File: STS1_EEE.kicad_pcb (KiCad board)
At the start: 4 copper layers, 81.1 x 85 mm, 43 parts, among them J1 Conn_02x20_Odd_Even, J2 Conn_02x20_Odd_Even, SW1 SW_SPST, U1 coordinate_system, U2 ST_Logo, U3 MP28167GQ, U4 1047

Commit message: Add EDU_HEARTBEAT adn EDU_UPDATE connections
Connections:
- J2 pad 37: unconnected-(J2-Pin_37-Pad37) -> EDU_Heartbeat
- J2 pad 39: unconnected-(J2-Pin_39-Pad39) -> EDU_UPDATE
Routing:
- net EDU_Heartbeat: track 2.00 -> 55.0 mm
- net EDU_UPDATE: track 2.00 -> 54.1 mm
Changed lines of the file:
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@@
 			(layers "*.Cu" "*.Mask")
 			(remove_unused_layers no)
-			(net "unconnected-(J2-Pin_37-Pad37)")
+			(net "EDU_Heartbeat")
 			(pinfunction "Pin_37_37")
-			(pintype "passive+no_connect")
+			(pintype "passive")
 		)
 		(pad "38" thru_hole circle
@@
 			(layers "*.Cu" "*.Mask")
 			(remove_unused_layers no)
-			(net "unconnected-(J2-Pin_39-Pad39)")
+			(net "EDU_UPDATE")
 			(pinfunction "Pin_39_39")
-			(pintype "passive+no_connect")
+			(pintype "passive")
 		)
 		(pad "40" thru_hole circle
@@
 		(sheetname "/powersupply/")
 		(sheetfile "powersupply.kicad_sch")
+		(units
+			(unit
+				(name "A")
+				(pins "1" "2" "3" "4")
+			)
+		)
 		(attr through_hole)
 		(duplicate_pad_numbers_are_jumpers no)
@@
 	)
 	(segment
+		(start 167.905 107.3)
+		(end 169.225 105.98)
+		(width 0.762)
+		(layer "B.Cu")
+		(net "EDU_Heartbeat")
+	)
+	(segment
+		(start 129.5 107.3)
+		(end 167.905 107.3)
+		(width 0.762)
+		(layer "B.Cu")
+		(net "EDU_Heartbeat")
+	)
+	(segment
+		(start 120.5 98.3)
+		(end 129.5 107.3)
+		(width 0.762)
+		(layer "B.Cu")
+		(net "EDU_Heartbeat")
+	)
+	(segment
 		(start 118.5 100.3)
 		(end 120.5 100.3)
@@
 		(net "EDU_UPDATE")
 	)
+	(segment
+		(start 128.72 108.52)
+		(end 169.225 108.52)
+		(width 0.762)
+		(layer "B.Cu")
+		(net "EDU_UPDATE")
+	)
+	(segment
+		(start 120.5 100.3)
+		(end 128.72 108.52)
+		(width 0.762)
+		(layer "B.Cu")
+		(net "EDU_UPDATE")
+	)

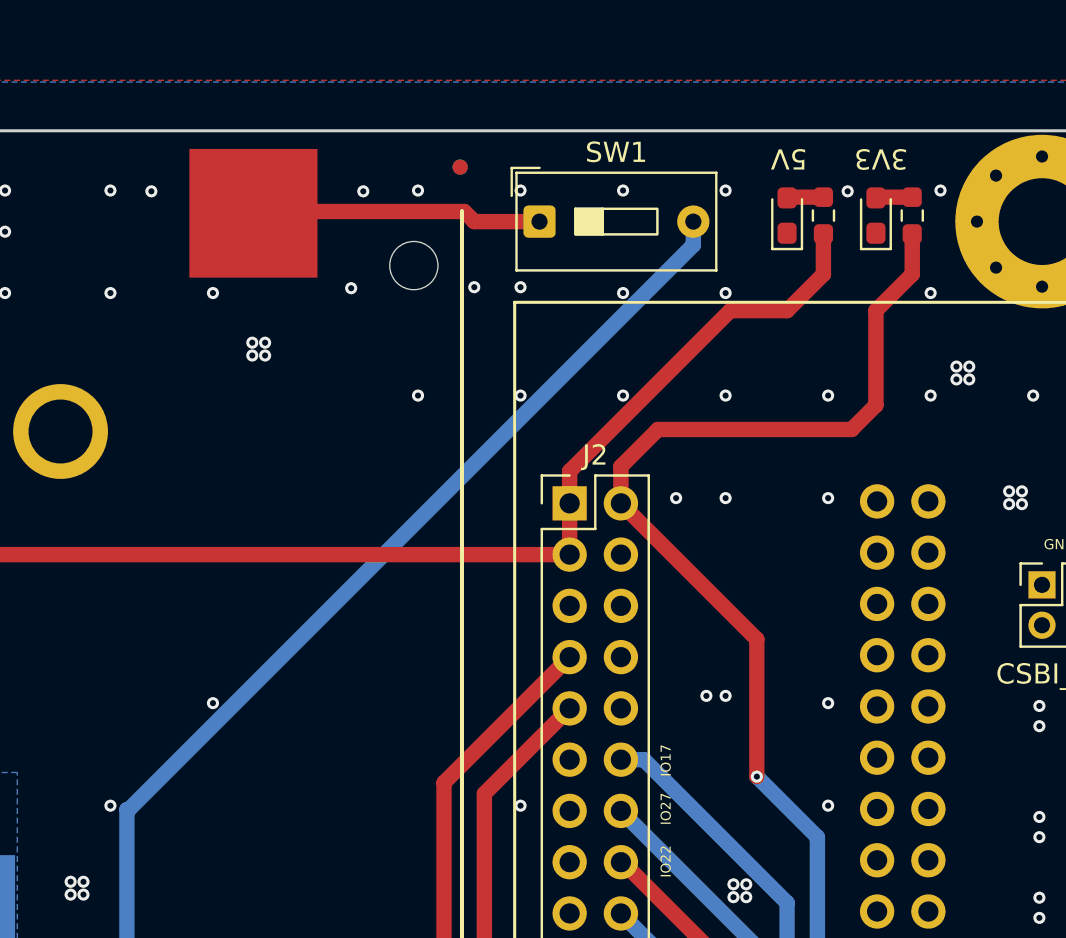
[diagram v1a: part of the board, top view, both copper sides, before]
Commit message: Replace the switch with the real one: 633-CS12ANW03
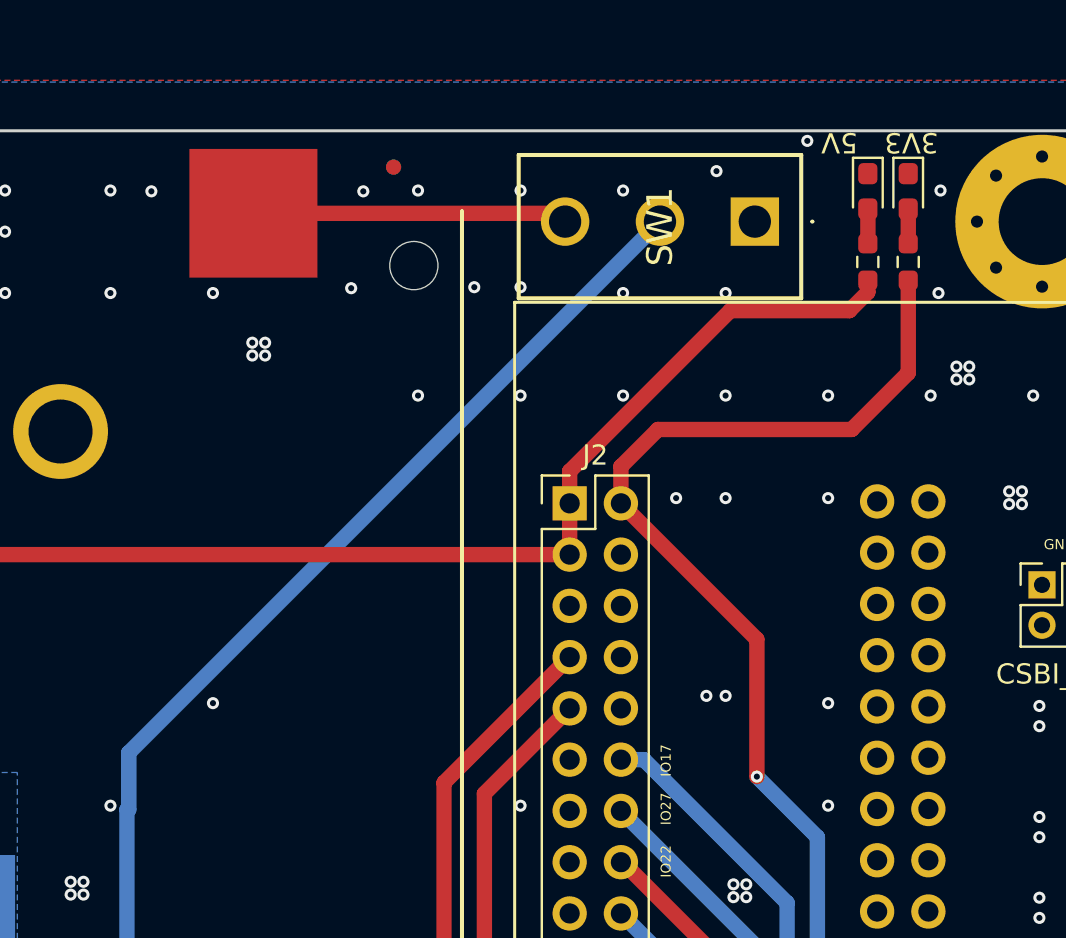
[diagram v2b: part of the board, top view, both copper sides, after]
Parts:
- SW1: footprint Button_Switch_THT:SW_DIP_SPSTx01_Slide_9.78x4.72mm_W7.62mm_P2.54mm -> STS_EEE:CS12ANW03
- moved SW1 10.7 mm to (178.4, 46.3), turned to 90 degrees
- moved D4 4.18 mm to (184.0, 44.8), turned to -90 degrees
- moved FID3 3.30 mm to (160.5, 43.6)
- moved FID4 3.30 mm to (160.5, 43.6)
- moved R4 3.18 mm to (184.0, 48.3)
- moved R3 2.31 mm to (186.0, 48.3)
- moved D3 2.00 mm to (186.0, 44.8), turned to -90 degrees
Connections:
- SW1 pad 1: Net-(SW1-A) -> unconnected-(SW1-NC-Pad1)
- U4 pad 3: Net-(SW1-A) -> Net-(SW1-NO)
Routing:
- net Net-(SW1-NO): track 0.00 -> 16.2 mm
- net Net-(SW1-A): track 14.5 -> 0.00 mm
- net Pi_3V3: track 97.4 -> 95.0 mm
- net VBAT: track 68.4 -> 67.7 mm

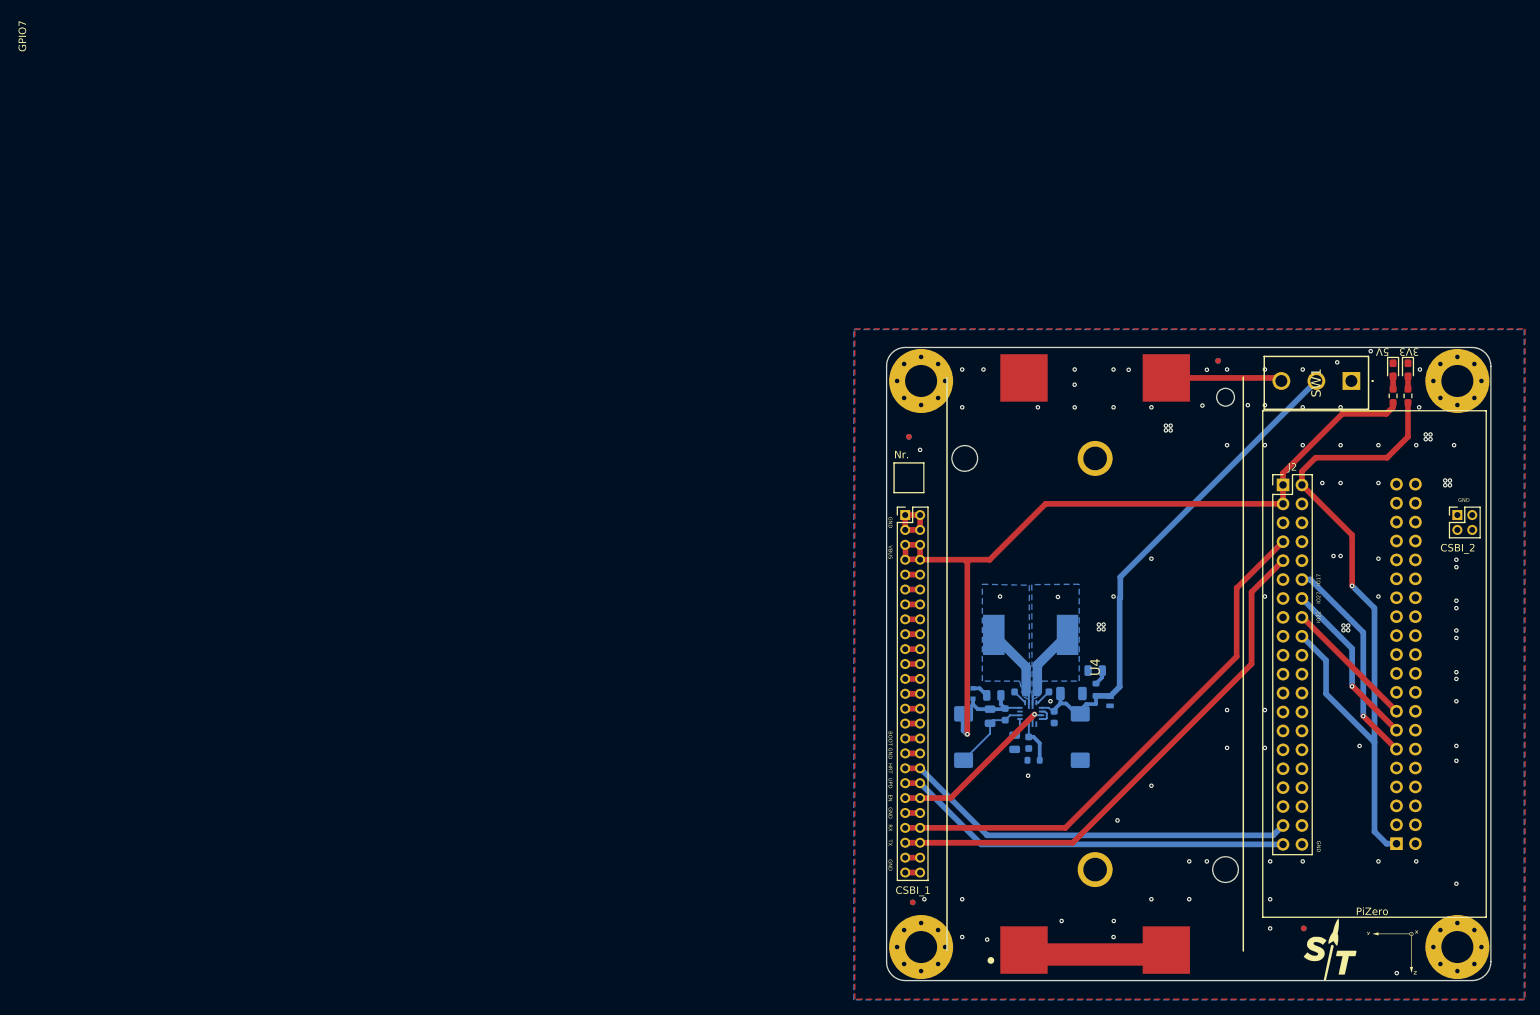
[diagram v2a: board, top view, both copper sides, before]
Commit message: Fix DRC errors and clean-up around the DC-DC circuit
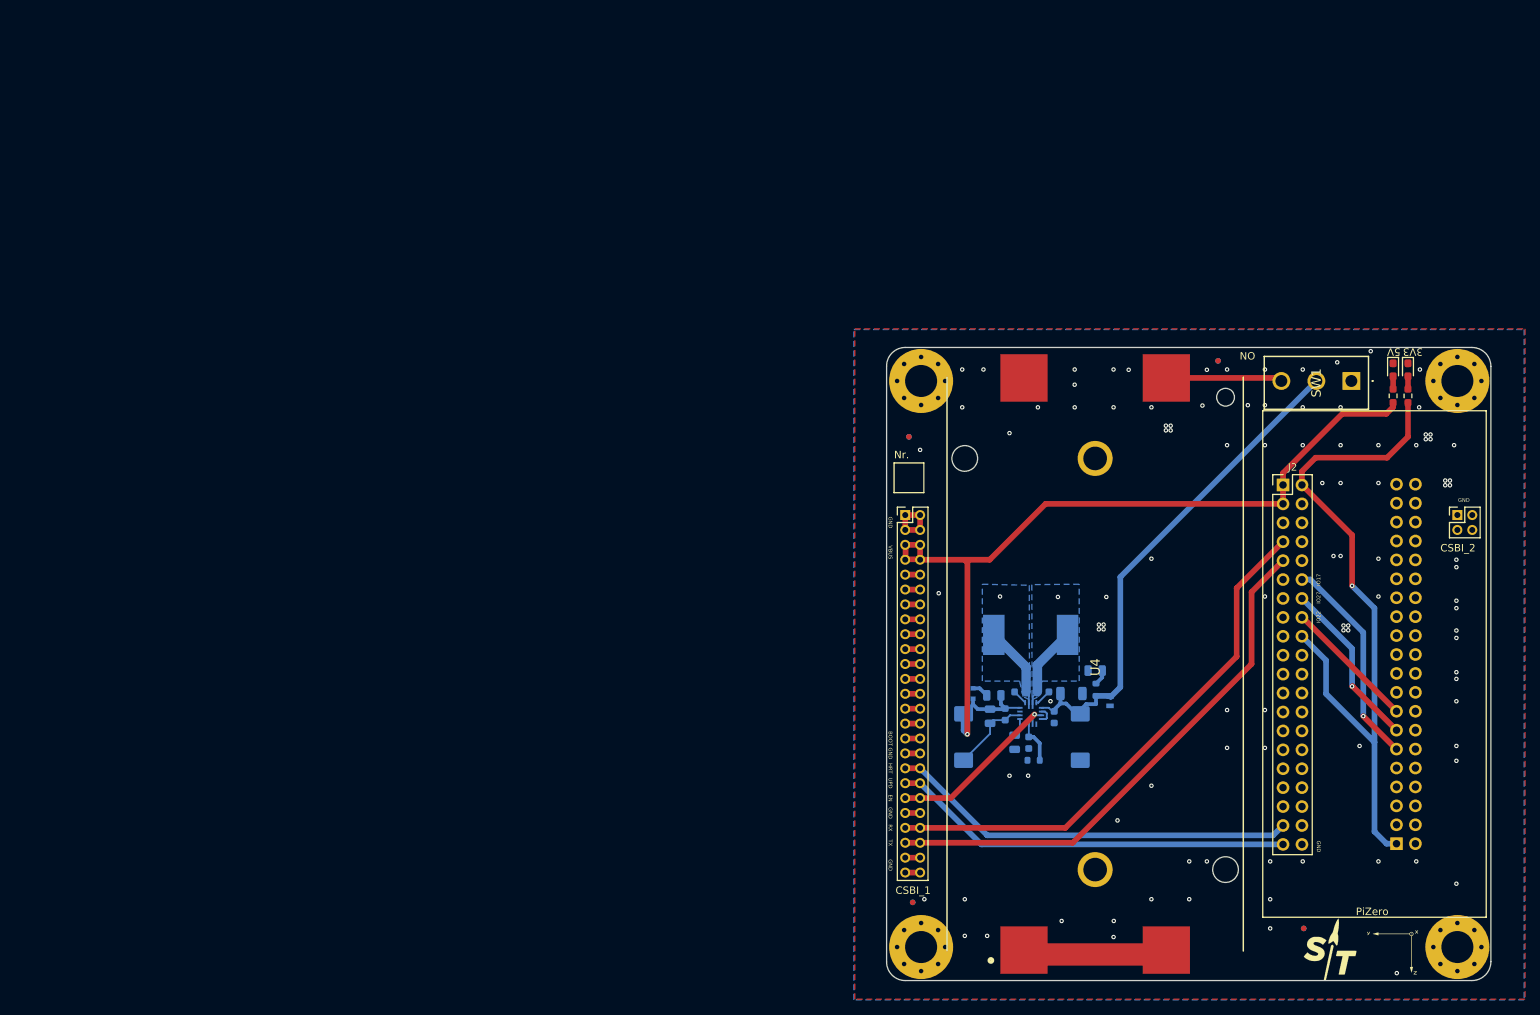
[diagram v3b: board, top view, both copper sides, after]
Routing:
- net GPIO27: vias 2 -> 1
- net GND: vias 103 -> 106
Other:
- rule pad_to_mask_clearance: 0.19 -> 0.05
- board text added: "ON"
- board text removed: "GPIO7"
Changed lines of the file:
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@@
 			(dielectric_constraints no)
 		)
-		(pad_to_mask_clearance 0.19)
+		(pad_to_mask_clearance 0.05)
 		(solder_mask_min_width 0.25)
 		(allow_soldermask_bridges_in_footprints no)
@@
 			(at 0 -1.68 90)
 			(layer "B.Fab")
+			(hide yes)
 			(effects
 				(font
@@
 			(at 0 -1.43 0)
 			(layer "B.Fab")
+			(hide yes)
 			(effects
 				(font
@@
 			)
 		)
-		(attr through_hole)
+		(attr smd)
 		(duplicate_pad_numbers_are_jumpers no)
 		(fp_line
@@
 			(at 0 -1.778 0)
 			(layer "B.SilkS")
+			(hide yes)
 			(effects
 				(font
@@
 			(at 0 -1.43 0)
 			(layer "B.Fab")
+			(hide yes)
 			(effects
 				(font
@@
 			(at 0 -1.43 90)
 			(layer "B.Fab")
+			(hide yes)
 			(effects
 				(font
@@
 			(at 0 2.54 0)
 			(layer "B.SilkS")
+			(hide yes)
 			(effects
 				(font
@@
 			(at 0 -1.68 0)
 			(layer "B.Fab")
+			(hide yes)
 			(effects
 				(font
@@
 			(at 0 1.778 0)
 			(layer "B.SilkS")
+			(hide yes)
 			(effects
 				(font
@@
 			(at 0 -1.43 0)
 			(layer "B.Fab")
+			(hide yes)
 			(effects
 				(font
@@
 			(at -0.254 -2.032 0)
 			(layer "B.SilkS")
+			(hide yes)
 			(effects
 				(font
@@
 			(at 0 -1.85 0)
 			(layer "B.Fab")
+			(hide yes)
 			(effects
 				(font
@@
 			(at 0 -3.1 90)
 			(layer "B.Fab")
+			(hide yes)
 			(effects
 				(font
@@
 			(at 0 -1.43 90)
 			(layer "B.Fab")
+			(hide yes)
 			(effects
 				(font
@@
 			(at 7.668 9.401411 90)
 			(layer "B.SilkS")
+			(hide yes)
 			(effects
 				(font
@@
 			(at 9.268 9.401411 90)
 			(layer "B.SilkS")
+			(hide yes)
 			(effects
 				(font
@@
 			)
 		)
-		(solder_mask_margin 0)
-		(attr smd)
+		(attr smd allow_soldermask_bridges)
 		(duplicate_pad_numbers_are_jumpers no)
 		(fp_line
@@
 		)
 	)
-	(gr_text "GPIO7"
-		(at 0 0 90)
+	(gr_text "ON"
+		(at 165.5 42.3 180)
 		(layer "F.SilkS")
 		(effects
@@
 				(thickness 0.15)
 			)
+			(justify left bottom)
 		)
 	)
 	(gr_text "5V"
-		(at 183.5 41.8 180)
+		(at 185 41.8 180)
 		(layer "F.SilkS")
 		(effects
@@
 	)
 	(gr_text "3V3"
-		(at 187.5 41.8 180)
+		(at 188 41.8 180)
 		(layer "F.SilkS")
 		(effects
@@
 	)
 	(via
+		(at 132.5 53.3)
+		(size 0.6)
+		(drill 0.3)
+		(layers "F.Cu" "B.Cu")
+		(free yes)
+		(net "GND")
+	)
+	(via
 		(at 187.5 49.84)
 		(size 0.6)
@@
 	)
 	(via
-		(at 129.5 121.3)
+		(at 129.5 120.8)
 		(size 0.6)
 		(drill 0.3)
@@
 	)
 	(via
-		(at 126.15175 115.88)
+		(at 126.5 115.88)
 		(size 0.6)
 		(drill 0.3)
@@
 	)
 	(via
-		(at 126.15175 120.96)
+		(at 126.5 120.8)
 		(size 0.6)
 		(drill 0.3)
@@
 	)
 	(via
-		(at 146.47175 75.24)
+		(at 145.5 75.3)
 		(size 0.6)
 		(drill 0.3)
@@
 	)
 	(via
+		(at 132.5 99.3)
+		(size 0.6)
+		(drill 0.3)
+		(layers "F.Cu" "B.Cu")
+		(free yes)
+		(capping no)
+		(covering
+			(front no)
+			(back no)
+		)
+		(plugging
+			(front no)
+			(back no)
+		)
+		(filling no)
+		(net "GND")
+	)
+	(via
 		(at 139.5 118.8)
 		(size 0.6)
@@
 	)
 	(via
+		(at 123 74.8)
+		(size 0.6)
+		(drill 0.3)
+		(layers "F.Cu" "B.Cu")
+		(free yes)
+		(capping no)
+		(covering
+			(front no)
+			(back no)
+		)
+		(plugging
+			(front no)
+			(back no)
+		)
+		(filling no)
+		(net "GND")
+	)
+	(via
 		(at 192.5 95.3)
 		(size 0.6)
@@
 	)
 	(via
-		(at 171.765 75.5)
-		(size 0.6)
-		(drill 0.3)
-		(layers "F.Cu" "B.Cu")
-		(net "GPIO27")
-	)
-	(via
 		(at 178.5 87.3)
 		(size 0.6)
@@
 	)
 	(segment
+		(start 168.59 45.89)
+		(end 169 46.3)
+		(width 0.762)
+		(layer "F.Cu")
+		(net "Net-(SW1-NO)")
+	)
+	(segment
+		(start 153.555 45.89)
+		(end 168.59 45.89)
+		(width 0.762)
+		(layer "F.Cu")
+		(net "Net-(SW1-NO)")
+	)
+	(segment
+		(start 153.945 45.8)
+		(end 153.555 45.41)
+		(width 0.762)
+		(layer "F.Cu")
+		(net "Net-(SW1-NO)")
+	)
+	(segment
+		(start 147.380446 72.619554)
+		(end 147.380446 87.419554)
+		(width 0.762)
+		(layer "B.Cu")
+		(net "VBAT")
+	)
+	(segment
 		(start 136.798932 90.183215)
 		(end 137.789931 90.183215)
@@
 	)
 	(segment
-		(start 147.289932 75.435805)
-		(end 147.380446 75.435805)
+		(start 173.7 46.3)
+		(end 147.380446 72.619554)
+		(width 0.762)
+		(layer "B.Cu")
+		(net "VBAT")
+	)
+	(segment
+		(start 147.380446 87.419554)
+		(end 146.1125 88.6875)
 		(width 0.762)
 		(layer "B.Cu")
@@
 	)
 	(segment
-		(start 147.380446 72.619554)
-		(end 173.7 46.3)
+		(start 146.1125 88.6875)
+		(end 146 88.6875)
 		(width 0.762)
 		(layer "B.Cu")
@@
 	)
 	(segment
-		(start 147.289932 75.435805)
-		(end 147.289932 87.373805)
-		(width 0.762)
-		(layer "B.Cu")
-		(net "VBAT")
-	)
-	(segment
 		(start 144.114932 88.579805)
 		(end 144.114932 89.688299)
@@
 	)
 	(segment
-		(start 147.289932 87.373805)
-		(end 146.083932 88.579805)
-		(width 0.762)
-		(layer "B.Cu")
-		(net "VBAT")
-	)
-	(segment
 		(start 139.337932 89.601216)
 		(end 140.094016 89.601216)
@@
 	)
 	(segment
-		(start 147.380446 75.435805)
-		(end 147.380446 72.619554)
-		(width 0.762)
-		(layer "B.Cu")
-		(net "VBAT")
-	)
-	(segment
 		(start 146.083932 88.579805)
 		(end 144.114932 88.579805)
@@
 		(net "Net-(U3-BST2)")
 	)
-	(segment
-		(start 168.59 45.89)
-		(end 169 46.3)
-		(width 0.762)
-		(layer "F.Cu")
-		(net "Net-(SW1-NO)")
-	)
-	(segment
-		(start 153.555 45.89)
-		(end 168.59 45.89)
-		(width 0.762)
-		(layer "F.Cu")
-		(net "Net-(SW1-NO)")
-	)
-	(segment
-		(start 153.945 45.8)
-		(end 153.555 45.41)
-		(width 0.762)
-		(layer "F.Cu")
-		(net "Net-(SW1-NO)")
-	)
 	(zone

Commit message: Set solder mask expansion to 0 mm as a global setting
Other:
- rule pad_to_mask_clearance: 0.05 -> 0
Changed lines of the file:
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@@
 			(dielectric_constraints no)
 		)
-		(pad_to_mask_clearance 0.05)
-		(solder_mask_min_width 0.25)
+		(pad_to_mask_clearance 0)
 		(allow_soldermask_bridges_in_footprints no)
 		(tenting
